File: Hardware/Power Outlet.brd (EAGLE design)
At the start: 160 x 100 mm, 28 parts, among them IC1 ATMega 328p-pu, IC2 ULN2003AD, K1 G5LE, K2 G5LE, Q1 16MHz

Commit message: initial mock up of board. added optocouplers to help increase isolation from mains
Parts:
- added C6: 1n/2Kv, rcl:C1206K
- added L1: (no value), rcl:L3225P
- added OK1, OK2: LTV816S, optocoupler:SMD4
- added R5, R6, R7, R8: 10k, rcl:R1206W
- C1: device rcl:153CLV-1010 -> rcl:E2,5-6E
- C2: device rcl:C025-025X050 -> rcl:C050-030X075
- moved LED2 215.0 mm to (129.5, 39.4)
- moved H2 211.1 mm to (154.9, 5.08)
- moved H3 203.3 mm to (156.2, 95.2)
- moved LED1 199.2 mm to (129.5, 57.1)
- moved S2 182.9 mm to (116.8, 34.3), turned to 90 degrees
- moved S1 166.5 mm to (116.8, 53.3), turned to 90 degrees
- moved C4 164.5 mm to (90.2, 7.62), flipped to the bottom
- moved R4 163.8 mm to (102.9, 5.08), flipped to the bottom
- moved Q1 159.7 mm to (83.8, 17.8), turned to 90 degrees
- moved R3 157.8 mm to (105.4, 10.2), flipped to the bottom
- moved SV1 157.2 mm to (99.1, 95.2)
- moved C3 148.8 mm to (88.9, 27.9), flipped to the bottom, turned to 180 degrees
- moved C5 144.5 mm to (72.4, 25.4), flipped to the bottom, turned to 270 degrees
- moved IC1 143.7 mm to (99.1, 30.5), turned to 270 degrees
- moved R2 127.8 mm to (81.3, 50.8), flipped to the bottom, turned to 90 degrees
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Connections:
- new net AGND: C6.2, IC2.5, IC2.6, IC2.7, IC2.8
- new net N$15: OK1.1, R5.1
- new net N$16: OK2.1, R6.1
- new net N$17: IC2.1, IC2.2, OK1.3
- new net N$18: IC2.3, IC2.4, OK2.3
- new net N$19: OK1.4, R7.2
- new net N$20: OK2.4, R8.2
- new net VCC: IC2.9, K1.1, K2.1, L1.2, R7.1, R8.1
- net +3V3: now also L1.1; no longer IC2.9, K1.1, K2.1
- net GND: now also C6.1, OK1.2, OK2.2; no longer IC2.5, IC2.6, IC2.7, IC2.8
- net OUT1_R: now also R6.2; no longer IC2.3, IC2.4
- net OUT2_R: now also R5.2; no longer IC2.1, IC2.2
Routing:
- added copper zone on layer 16, net GND

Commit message: started routing wires
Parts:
- moved SV1 86.5 mm to (154.9, 29.2), turned to 270 degrees
- moved R3 42.1 mm to (125.7, 47.0), turned to 270 degrees
- moved R4 32.3 mm to (125.7, 27.9), turned to 270 degrees
- moved C1 18.2 mm to (82.5, 33.0)
- moved C5 17.0 mm to (87.6, 33.0)
- moved C4 12.8 mm to (88.9, 20.3), turned to 270 degrees
- moved L1 12.5 mm to (59.7, 44.5)
- moved R2 7.41 mm to (87.6, 47.0), turned to 0 degrees
- moved LED2 5.24 mm to (128.3, 34.3)
- moved Q1 5.08 mm to (83.8, 22.9)
- moved LED1 4.02 mm to (128.3, 53.3)
- moved C3 1.27 mm to (88.9, 26.7), turned to 90 degrees
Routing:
- net +3V3: track 0.00 -> 60.2 mm
- net GND: track 0.00 -> 30.7 mm
- net N$6: track 0.00 -> 11.7 mm
- net N$5: track 0.00 -> 10.8 mm
- net N$4: track 0.00 -> 4.85 mm

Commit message: Finilised Rev A. Power Outlet Board
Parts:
- removed X4, X5, X6: (no value), con-wago-500:W237-103
- added X1: VIN, con-wago-500:W237-102
- added X2: VOUT2, con-wago-500:W237-102
- added X3: VOUT1, con-wago-500:W237-102
- added X7: EARTH, con-wago-500:W237-103
- moved LED1 58.5 mm to (95.2, 5.08), turned to 270 degrees
- moved LED2 50.0 mm to (87.6, 5.08), turned to 270 degrees
- moved R3 48.5 mm to (92.7, 11.4), turned to 90 degrees
- moved S2 48.4 mm to (113.0, 82.5)
- moved R4 42.7 mm to (86.4, 11.4), turned to 90 degrees
- moved S1 34.9 mm to (97.8, 82.5)
- moved H3 24.1 mm to (132.1, 95.2)
- moved H2 22.9 mm to (132.1, 3.81)
- moved SV1 22.9 mm to (132.1, 29.2)
- moved R5 14.9 mm to (91.4, 66.0), turned to 270 degrees
- moved F1 14.2 mm to (16.5, 22.9), turned to 270 degrees
- moved K2 12.7 mm to (30.5, 77.5)
- moved R6 6.48 mm to (86.4, 66.0), turned to 270 degrees
- moved C4 5.24 mm to (83.8, 19.1)
- moved R8 5.24 mm to (68.6, 77.5), turned to 270 degrees
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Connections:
- net GND1: now also X7.1, X7.2, X7.3; no longer X4.3, X5.3, X6.3
- net N$1: now also X1.1; no longer X4.1
- net N$11: now also X2.1; no longer X5.1
- net N$14: now also X3.1; no longer X6.1
- net N$3: now also X1.2, X2.2, X3.2; no longer X4.2, X5.2, X6.2
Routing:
- net N$3: track 0.00 -> 176.7 mm
- net VCC: track 0.00 -> 126.6 mm
- net N$1: track 0.00 -> 103.4 mm
- net +3V3: track 60.2 -> 120.4 mm, vias 0 -> 2
- net N$10: track 0.00 -> 49.7 mm
- net N$9: track 0.00 -> 45.7 mm
- net INT: track 0.00 -> 42.2 mm
- net MOSI: track 0.00 -> 40.4 mm
- net CSN2: track 0.00 -> 39.0 mm
- net OUT1_R: track 0.00 -> 36.9 mm, vias 0 -> 2
- net N$2: track 0.00 -> 35.9 mm
- net RXD: track 0.00 -> 35.9 mm
- net TXD: track 0.00 -> 35.9 mm
- net CSN: track 0.00 -> 31.0 mm
- net CE: track 0.00 -> 31.0 mm
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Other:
- board size 160 x 100 mm -> 138.4 x 100 mm
- board text added: "2015"
- board text added: "Outlet 1"
- board text added: "Outlet 2"
- board text added: "Power Outlet Rev A"
- board text added: "SmartHome"

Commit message: updated Fuse Holder for part that is in stock. Updated wrong Processor footprint also fixed screw terminals wrong way round
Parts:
- F1: device fuse:GSH15 -> fuse:SH22,5A
- IC1: device ic-package:DIL28-4 -> ic-package:DIL28-3
- moved X1 2.54 mm to (12.7, 43.2), turned to 270 degrees
- moved X2 2.54 mm to (12.7, 68.6), turned to 270 degrees
- moved X3 2.54 mm to (12.7, 55.9), turned to 270 degrees
- moved X7 2.54 mm to (12.7, 82.5), turned to 270 degrees
- moved F1 1.27 mm to (16.5, 24.1)
- moved R6 1.27 mm to (85.1, 66.0)
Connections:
- net N$1: now also X1.2; no longer X1.1
- net N$11: now also X2.2; no longer X2.1
- net N$14: now also X3.2; no longer X3.1
- net N$3: now also X1.1, X2.1, X3.1; no longer X1.2, X2.2, X3.2
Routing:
- net N$1: track 103.4 -> 98.8 mm
- net OUT1_R: track 36.9 -> 40.2 mm
- net N$3: track 176.7 -> 174.7 mm
- net GND: track 55.9 -> 57.7 mm
- net N$6: track 15.5 -> 16.8 mm
- net TXD: track 35.9 -> 34.6 mm
- net SCK: track 24.7 -> 25.9 mm
- net RXD: track 35.9 -> 34.6 mm
- net OUT2_R: track 29.3 -> 30.6 mm
- net OUT2_LED: track 8.97 -> 10.2 mm
- net OUT1_LED: track 15.0 -> 16.3 mm
- net N$5: track 10.8 -> 12.1 mm
- net N$4: track 4.85 -> 6.12 mm
- net N$10: track 49.7 -> 50.9 mm
- net MOSI: track 40.4 -> 39.1 mm
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
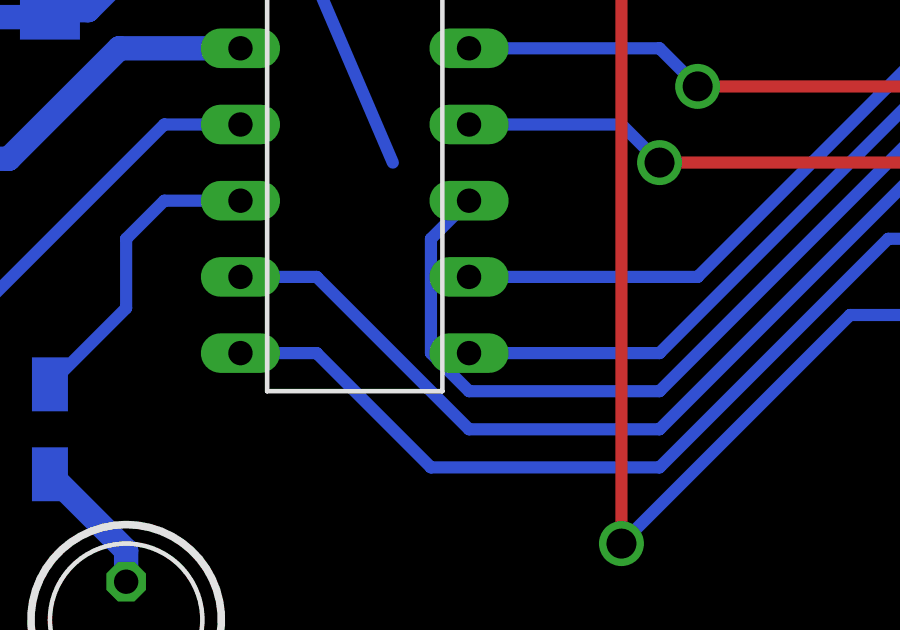
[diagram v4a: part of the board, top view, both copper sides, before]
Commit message: updated crossed paths from last update
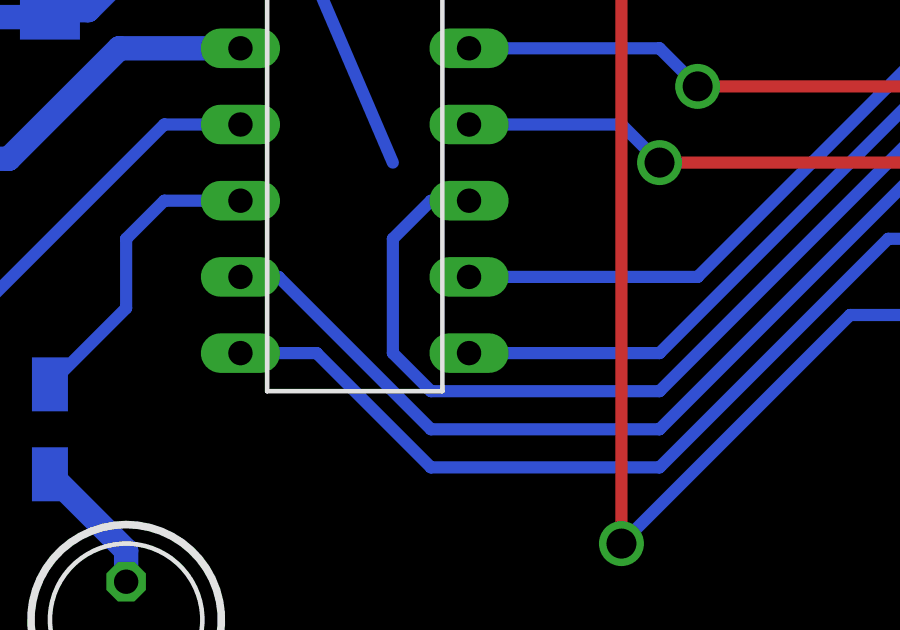
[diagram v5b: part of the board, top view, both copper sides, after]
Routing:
- net MOSI: track 39.1 -> 41.7 mm
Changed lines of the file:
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@@
 <contactref element="IC1" pad="13"/>
 <contactref element="SV1" pad="8"/>
-<wire x1="99.06" y1="16.51" x2="101.6" y2="16.51" width="0.4064" layer="16"/>
-<wire x1="101.6" y1="16.51" x2="106.68" y2="11.43" width="0.4064" layer="16"/>
-<wire x1="106.68" y1="11.43" x2="113.03" y2="11.43" width="0.4064" layer="16"/>
+<wire x1="99.06" y1="16.51" x2="100.33" y2="16.51" width="0.4064" layer="16"/>
+<wire x1="100.33" y1="16.51" x2="105.41" y2="11.43" width="0.4064" layer="16"/>
+<wire x1="105.41" y1="11.43" x2="113.03" y2="11.43" width="0.4064" layer="16"/>
 <wire x1="113.03" y1="11.43" x2="127" y2="25.4" width="0.4064" layer="16"/>
 <wire x1="127" y1="25.4" x2="132.08" y2="25.4" width="0.4064" layer="16"/>
@@
 <wire x1="132.08" y1="27.94" x2="128.27" y2="27.94" width="0.4064" layer="16"/>
 <wire x1="128.27" y1="27.94" x2="113.03" y2="12.7" width="0.4064" layer="16"/>
-<wire x1="113.03" y1="12.7" x2="106.68" y2="12.7" width="0.4064" layer="16"/>
-<wire x1="106.68" y1="12.7" x2="105.41" y2="13.97" width="0.4064" layer="16"/>
-<wire x1="105.41" y1="13.97" x2="105.41" y2="17.78" width="0.4064" layer="16"/>
-<wire x1="105.41" y1="17.78" x2="106.68" y2="19.05" width="0.4064" layer="16"/>
+<wire x1="113.03" y1="12.7" x2="105.41" y2="12.7" width="0.4064" layer="16"/>
+<wire x1="105.41" y1="12.7" x2="104.14" y2="13.97" width="0.4064" layer="16"/>
+<wire x1="104.14" y1="13.97" x2="104.14" y2="17.78" width="0.4064" layer="16"/>
+<wire x1="104.14" y1="17.78" x2="105.41" y2="19.05" width="0.4064" layer="16"/>
+<wire x1="105.41" y1="19.05" x2="106.68" y2="19.05" width="0.4064" layer="16"/>
 </signal>
 <signal name="CE">

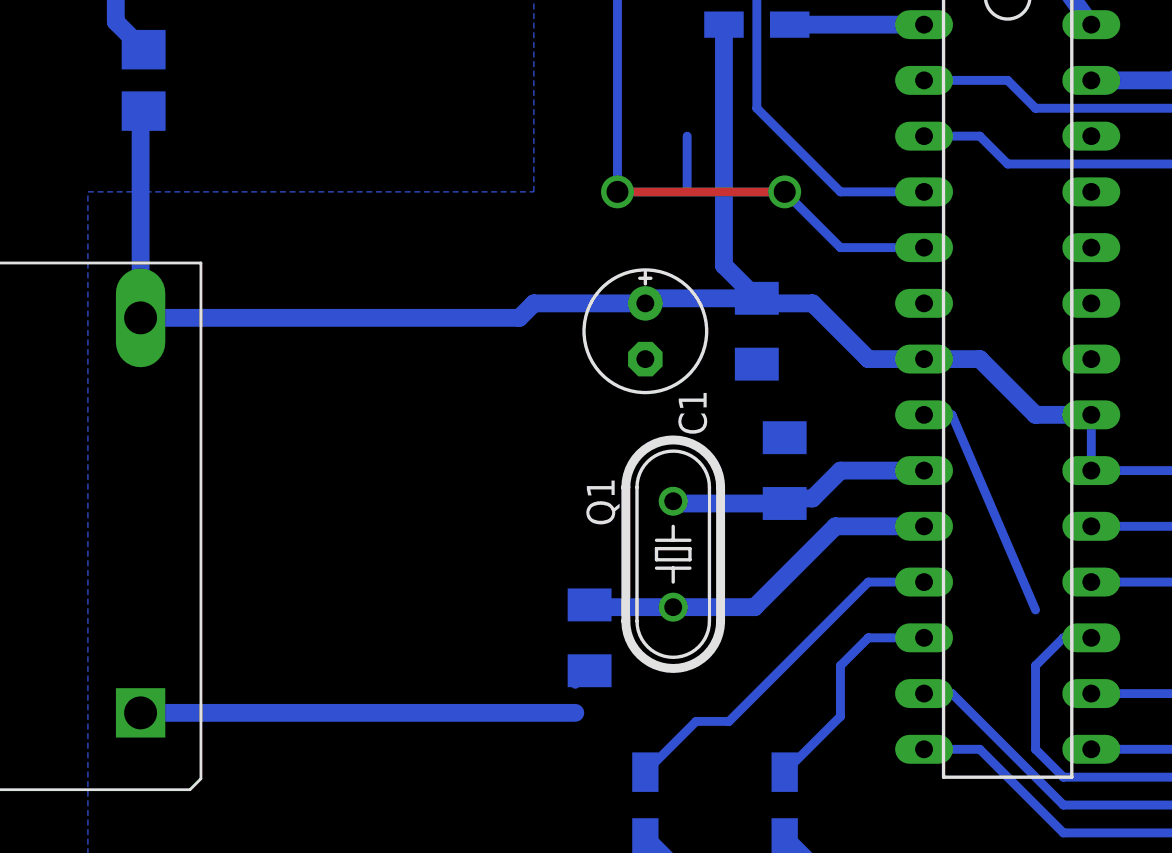
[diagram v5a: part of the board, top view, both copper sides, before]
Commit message: updated to correct componnent values and minor tweaks
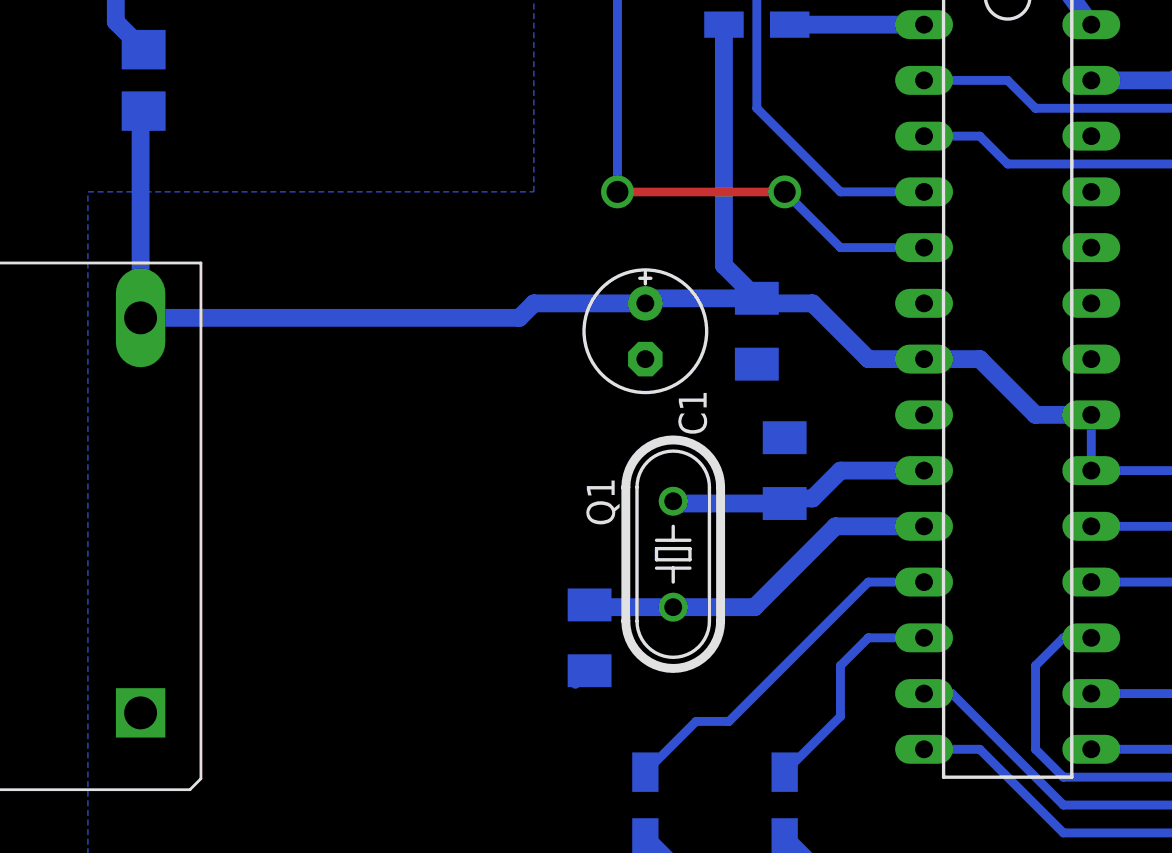
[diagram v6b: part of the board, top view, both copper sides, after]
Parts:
- C1: value 10u -> 47u
- C5: value 1n -> 0.1u
- Q1: value 16MHz -> 8MHz
- R3, R4: value 330R -> 3k3
- R5, R6, R7, R8: value 10k -> 100R
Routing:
- net GND: track 57.7 -> 24.5 mm
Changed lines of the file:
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@@
 </element>
 <element name="R1" library="varistor" package="P594" value="P594" x="27.94" y="26.67"/>
-<element name="C1" library="rcl" package="E2,5-6E" value="10u" x="86.36" y="33.02" rot="R270"/>
+<element name="C1" library="rcl" package="E2,5-6E" value="47u" x="86.36" y="33.02" rot="R270"/>
 <element name="C2" library="rcl" package="C050-030X075" value="0.1u/275V" x="36.83" y="25.4" rot="R90"/>
 <element name="K1" library="relay" package="G5LE" value="G5LE" x="45.72" y="53.34" rot="R270">
@@
 </element>
 <element name="IC1" library="ic-package" package="DIL28-3" value="ATMega 328p-pu" x="102.87" y="30.48" rot="R270"/>
-<element name="Q1" library="crystal" package="HC49/S" value="16MHz" x="87.63" y="22.86" smashed="yes" rot="R90">
+<element name="Q1" library="crystal" package="HC49/S" value="8MHz" x="87.63" y="22.86" smashed="yes" rot="R90">
 <attribute name="OC_NEWARK" value="unknown" x="163.83" y="87.63" size="1.778" layer="27" rot="R90" display="off"/>
 <attribute name="MPN" value="" x="163.83" y="87.63" size="1.778" layer="27" rot="R90" display="off"/>
@@
 </element>
 <element name="R2" library="rcl" package="R1206W" value="10k" x="91.44" y="46.99" rot="MR0"/>
-<element name="R3" library="rcl" package="R1206W" value="330R" x="92.71" y="11.43" rot="MR90"/>
-<element name="R4" library="rcl" package="R1206W" value="330R" x="86.36" y="11.43" rot="MR90"/>
+<element name="R3" library="rcl" package="R1206W" value="3k3" x="92.71" y="11.43" rot="MR90"/>
+<element name="R4" library="rcl" package="R1206W" value="3k3" x="86.36" y="11.43" rot="MR90"/>
 <element name="C3" library="rcl" package="C1206K" value="22p" x="92.71" y="26.67" rot="MR90"/>
 <element name="C4" library="rcl" package="C1206K" value="22p" x="83.82" y="19.05" smashed="yes" rot="MR270">
@@
 <attribute name="VALUE" x="85.92" y="20.65" size="1.016" layer="28" rot="MR270"/>
 </element>
-<element name="C5" library="rcl" package="C1206K" value="1n" x="91.44" y="33.02" rot="MR270"/>
+<element name="C5" library="rcl" package="C1206K" value="0.1u" x="91.44" y="33.02" rot="MR270"/>
 <element name="IC2" library="uln-udn" package="SO16" value="ULN2003AD" x="62.23" y="66.04" smashed="yes" rot="MR270">
 <attribute name="VALUE" x="62.865" y="70.104" size="1.27" layer="28" ratio="10" rot="MR270"/>
@@
 <attribute name="OC_FARNELL" value="unknown" x="78.74" y="71.12" size="1.778" layer="28" rot="MR270" display="off"/>
 </element>
-<element name="R5" library="rcl" package="R1206W" value="10k" x="91.44" y="66.04" rot="MR270"/>
-<element name="R6" library="rcl" package="R1206W" value="10k" x="85.09" y="66.04" rot="MR270"/>
+<element name="R5" library="rcl" package="R1206W" value="100R" x="91.44" y="66.04" rot="MR270"/>
+<element name="R6" library="rcl" package="R1206W" value="100R" x="85.09" y="66.04" rot="MR270"/>
 <element name="L1" library="rcl" package="L3225P" value="" x="63.5" y="44.45" rot="MR90"/>
 <element name="C6" library="rcl" package="C1206K" value="1n/2Kv" x="77.47" y="60.96" rot="MR0"/>
-<element name="R7" library="rcl" package="R1206W" value="10k" x="69.85" y="81.28" smashed="yes" rot="MR180">
+<element name="R7" library="rcl" package="R1206W" value="100R" x="69.85" y="81.28" smashed="yes" rot="MR180">
 <attribute name="NAME" x="69.215" y="83.82" size="1.27" layer="26" rot="MR180"/>
 <attribute name="VALUE" x="67.945" y="83.82" size="1.27" layer="28" rot="MR180"/>
 </element>
-<element name="R8" library="rcl" package="R1206W" value="10k" x="68.58" y="77.47" smashed="yes" rot="MR270">
+<element name="R8" library="rcl" package="R1206W" value="100R" x="68.58" y="77.47" smashed="yes" rot="MR270">
 <attribute name="NAME" x="71.12" y="74.295" size="1.27" layer="26" rot="MR270"/>
 <attribute name="VALUE" x="71.12" y="79.375" size="1.27" layer="28" rot="MR270"/>
@@
 <vertex x="81.28" y="100.33"/>
 </polygon>
-<wire x1="63.36" y1="15.63" x2="83.17" y2="15.63" width="0.8128" layer="16"/>
 <wire x1="82.24" y1="64.23" x2="82.24" y2="69.85" width="0.4064" layer="16"/>
 <wire x1="83.82" y1="17.55" x2="83.17" y2="16.93" width="0.4064" layer="16"/>
 <wire x1="82.24" y1="64.23" x2="82.78" y2="66.04" width="0.4064" layer="16"/>
 <wire x1="82.78" y1="66.04" x2="95.25" y2="66.04" width="0.4064" layer="16"/>
-<wire x1="99.06" y1="29.21" x2="100.33" y2="29.21" width="0.4064" layer="16"/>
-<wire x1="100.33" y1="29.21" x2="104.14" y2="20.32" width="0.4064" layer="16"/>
 <wire x1="78.97" y1="60.96" x2="82.55" y2="60.96" width="0.8128" layer="16"/>
-<wire x1="88.265" y1="39.37" x2="88.265" y2="41.91" width="0.4064" layer="16"/>
 </signal>
 <signal name="N$4">

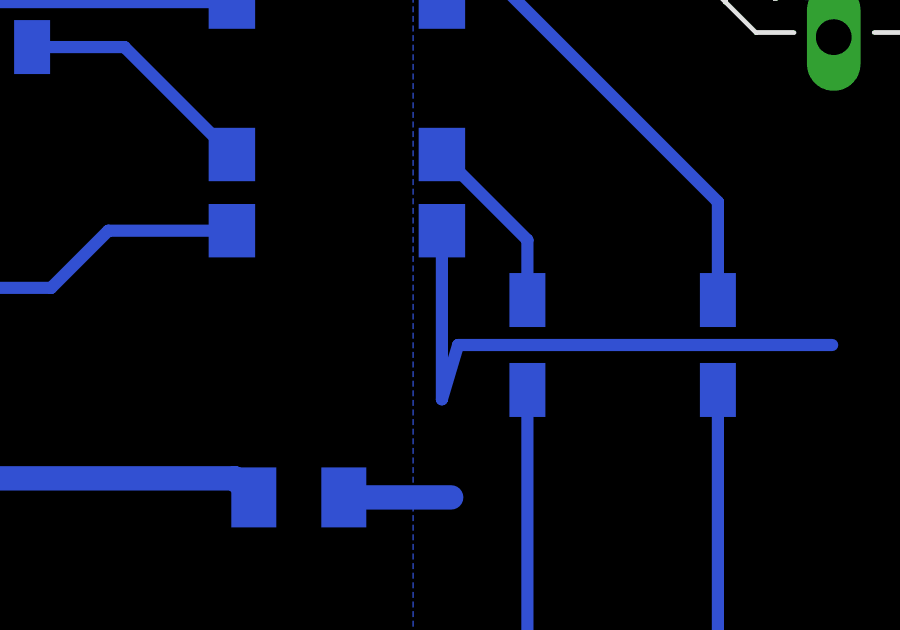
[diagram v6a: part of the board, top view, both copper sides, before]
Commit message: cleaned Rev A. traces before archive.
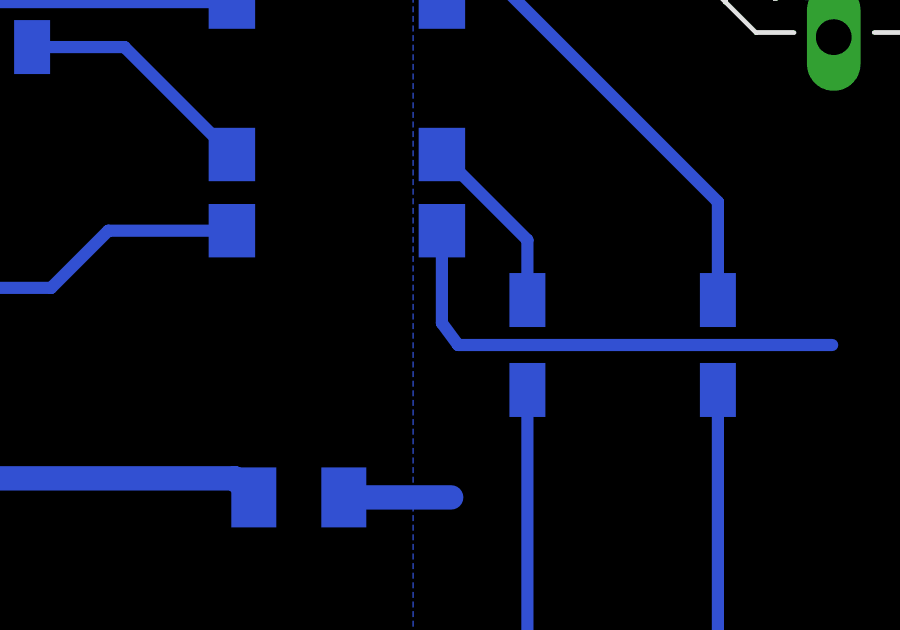
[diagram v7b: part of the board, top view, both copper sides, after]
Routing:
- net GND: track 24.5 -> 20.9 mm
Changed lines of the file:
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@@
 <vertex x="81.28" y="100.33"/>
 </polygon>
-<wire x1="82.24" y1="64.23" x2="82.24" y2="69.85" width="0.4064" layer="16"/>
+<wire x1="82.24" y1="66.77" x2="82.24" y2="69.85" width="0.4064" layer="16"/>
 <wire x1="83.82" y1="17.55" x2="83.17" y2="16.93" width="0.4064" layer="16"/>
-<wire x1="82.24" y1="64.23" x2="82.78" y2="66.04" width="0.4064" layer="16"/>
+<wire x1="82.24" y1="66.77" x2="82.78" y2="66.04" width="0.4064" layer="16"/>
 <wire x1="82.78" y1="66.04" x2="95.25" y2="66.04" width="0.4064" layer="16"/>
 <wire x1="78.97" y1="60.96" x2="82.55" y2="60.96" width="0.8128" layer="16"/>
